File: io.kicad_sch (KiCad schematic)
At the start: 67 parts, among them J10 JP_REL1_COM_12V, J12 JP_REL2_COM_12V, J13 JP_REL3_COM_12V, J14 Conn_REL1, J15 Conn_REL2, J16 Conn_REL3, J5 JP_REL4_COM_12V, J8 JP_REL5_COM_12V, J9 JP_REL6_COM_12V, K2 TIANBO-HJR-4102-L, K3 TIANBO-HJR-4102-L, K4 TIANBO-HJR-4102-L, K5 TIANBO-HJR-4102-L, K6 TIANBO-HJR-4102-L, K7 TIANBO-HJR-4102-L, Q2 BSS138, Q3 BSS138, Q4 BSS138, Q5 BSS138, Q6 BSS138, Q7 BSS138, U10 74HC595, U20 HC 151, X5 Conn_Rel2, X6 Conn_Rel1

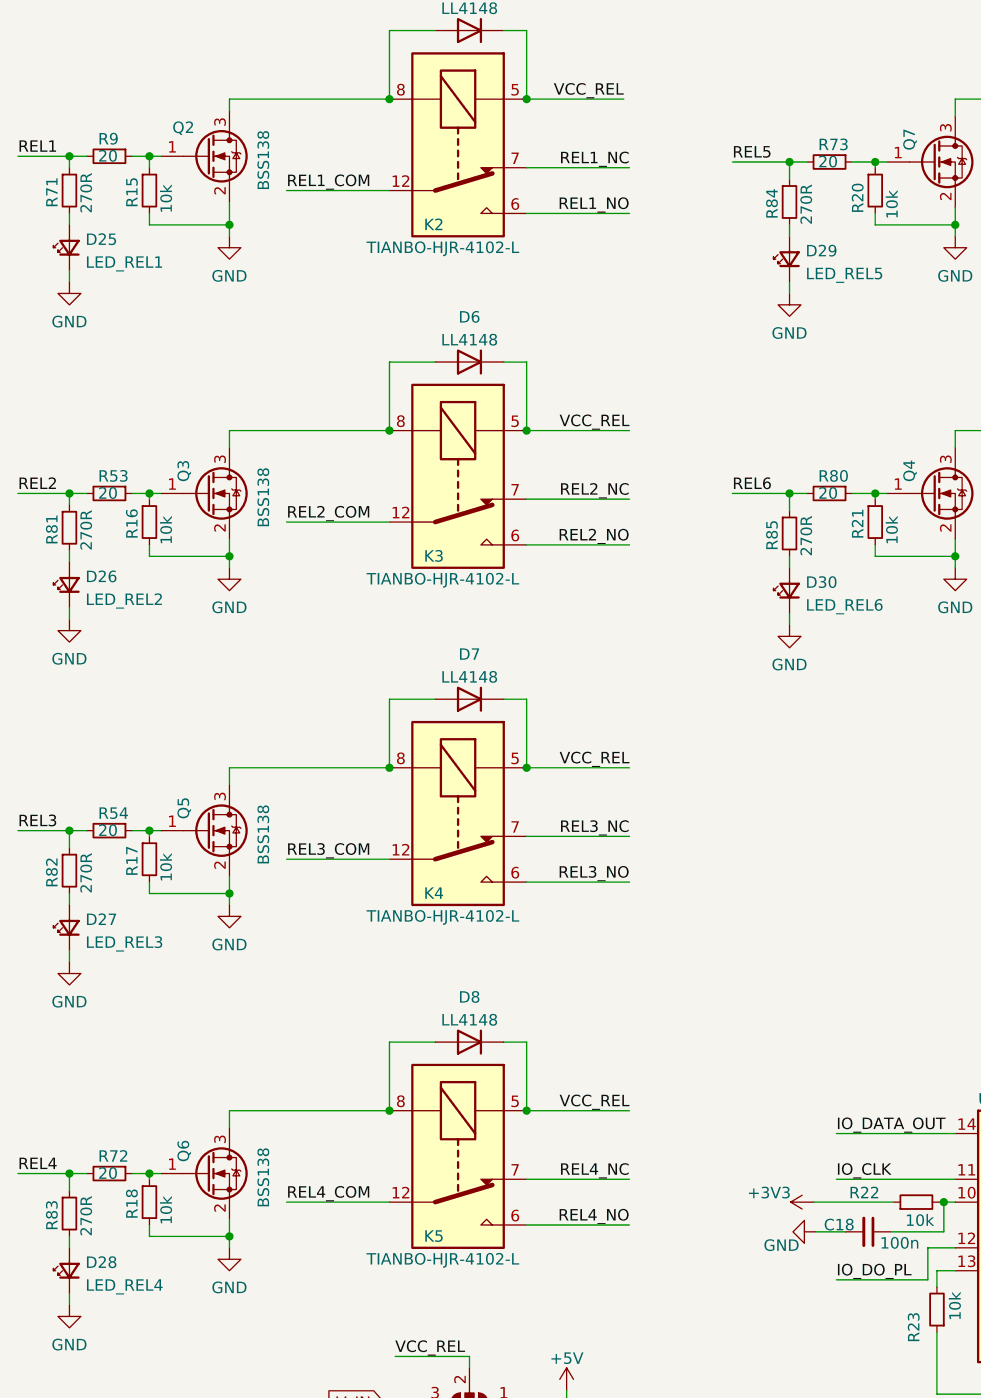
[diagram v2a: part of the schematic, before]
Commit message: Change extension bus
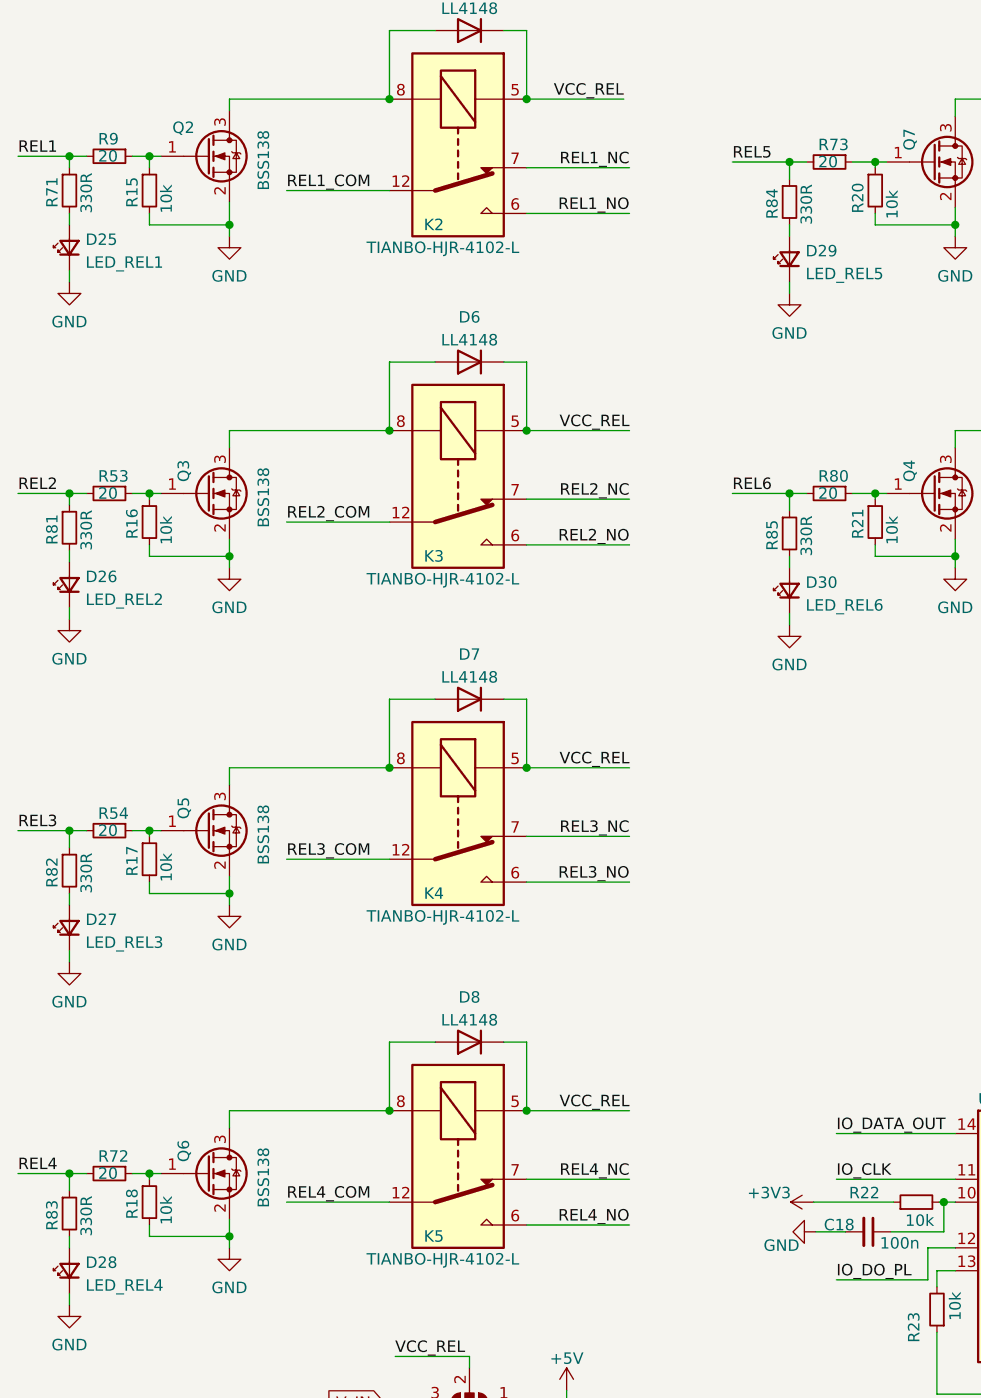
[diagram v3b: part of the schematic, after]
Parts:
- J10, J12, J13, J5, J8, J9: footprint Connector_PinHeader_2.54mm:PinHeader_1x02_P2.54mm_Vertical -> custom_th:PinHeader_1x02_P2.54mm_Vertical_jlc
- J14, J15, J16: footprint Connector_PinHeader_2.54mm:PinHeader_1x03_P2.54mm_Vertical -> custom_th:PinHeader_1x03_P2.54mm_Vertical_jlc
- R71, R81, R82, R83, R84, R85: value 270R -> 330R
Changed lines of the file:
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@@
   (title_block
     (title "BSC")
-    (date "2022-12-16")
-    (rev "2.1")
+    (date "2023-03-30")
+    (rev "2.3")
   )
   (junction (at 128.905 174.371) (diameter 0) (color 0 0 0 0)
@@
     (property "Reference" "J9" (id 0) (at 184.785 72.39 0))
     (property "Value" "JP_REL6_COM_12V" (id 1) (at 187.325 69.215 0))
-    (property "Footprint" "Connector_PinHeader_2.54mm:PinHeader_1x02_P2.54mm_Vertical" (id 2) (at 188.595 70.485 0)
+    (property "Footprint" "custom_th:PinHeader_1x02_P2.54mm_Vertical_jlc" (id 2) (at 188.595 70.485 0)
       (effects (font (size 1.27 1.27)) hide)
     )
@@
       (effects (font (size 1.27 1.27)) (justify left))
     )
-    (property "Value" "270R" (id 1) (at 22.225 118.745 90)
+    (property "Value" "330R" (id 1) (at 22.225 118.745 90)
       (effects (font (size 1.27 1.27)) (justify left))
     )
@@
     (property "Reference" "J12" (id 0) (at 184.785 38.735 0))
     (property "Value" "JP_REL2_COM_12V" (id 1) (at 187.96 36.195 0))
-    (property "Footprint" "Connector_PinHeader_2.54mm:PinHeader_1x02_P2.54mm_Vertical" (id 2) (at 189.23 37.465 0)
+    (property "Footprint" "custom_th:PinHeader_1x02_P2.54mm_Vertical_jlc" (id 2) (at 189.23 37.465 0)
       (effects (font (size 1.27 1.27)) hide)
     )
@@
       (effects (font (size 1.27 1.27)) (justify left))
     )
-    (property "Value" "270R" (id 1) (at 102.235 81.28 90)
+    (property "Value" "330R" (id 1) (at 102.235 81.28 90)
       (effects (font (size 1.27 1.27)) (justify left))
     )
@@
     (property "Reference" "J10" (id 0) (at 184.785 30.48 0))
     (property "Value" "JP_REL1_COM_12V" (id 1) (at 187.96 27.94 0))
-    (property "Footprint" "Connector_PinHeader_2.54mm:PinHeader_1x02_P2.54mm_Vertical" (id 2) (at 189.23 29.21 0)
+    (property "Footprint" "custom_th:PinHeader_1x02_P2.54mm_Vertical_jlc" (id 2) (at 189.23 29.21 0)
       (effects (font (size 1.27 1.27)) hide)
     )
@@
     (property "Reference" "J8" (id 0) (at 184.785 63.5 0))
     (property "Value" "JP_REL5_COM_12V" (id 1) (at 187.325 60.96 0))
-    (property "Footprint" "Connector_PinHeader_2.54mm:PinHeader_1x02_P2.54mm_Vertical" (id 2) (at 188.595 62.23 0)
+    (property "Footprint" "custom_th:PinHeader_1x02_P2.54mm_Vertical_jlc" (id 2) (at 188.595 62.23 0)
       (effects (font (size 1.27 1.27)) hide)
     )
@@
     (property "Reference" "J5" (id 0) (at 184.785 55.245 0))
     (property "Value" "JP_REL4_COM_12V" (id 1) (at 187.325 52.705 0))
-    (property "Footprint" "Connector_PinHeader_2.54mm:PinHeader_1x02_P2.54mm_Vertical" (id 2) (at 188.595 53.975 0)
+    (property "Footprint" "custom_th:PinHeader_1x02_P2.54mm_Vertical_jlc" (id 2) (at 188.595 53.975 0)
       (effects (font (size 1.27 1.27)) hide)
     )
@@
     (property "Reference" "J16" (id 0) (at 216.535 98.425 0))
     (property "Value" "Conn_REL3" (id 1) (at 212.725 102.87 0))
-    (property "Footprint" "Connector_PinHeader_2.54mm:PinHeader_1x03_P2.54mm_Vertical" (id 2) (at 213.36 98.425 0)
+    (property "Footprint" "custom_th:PinHeader_1x03_P2.54mm_Vertical_jlc" (id 2) (at 213.36 98.425 0)
       (effects (font (size 1.27 1.27)) hide)
     )
@@
     (property "Reference" "J14" (id 0) (at 216.535 121.285 0))
     (property "Value" "Conn_REL1" (id 1) (at 212.725 125.73 0))
-    (property "Footprint" "Connector_PinHeader_2.54mm:PinHeader_1x03_P2.54mm_Vertical" (id 2) (at 213.36 121.285 0)
+    (property "Footprint" "custom_th:PinHeader_1x03_P2.54mm_Vertical_jlc" (id 2) (at 213.36 121.285 0)
       (effects (font (size 1.27 1.27)) hide)
     )
@@
       (effects (font (size 1.27 1.27)) (justify left))
     )
-    (property "Value" "270R" (id 1) (at 22.225 156.845 90)
+    (property "Value" "330R" (id 1) (at 22.225 156.845 90)
       (effects (font (size 1.27 1.27)) (justify left))
     )
@@
       (effects (font (size 1.27 1.27)) (justify left))
     )
-    (property "Value" "270R" (id 1) (at 102.235 44.45 90)
+    (property "Value" "330R" (id 1) (at 102.235 44.45 90)
       (effects (font (size 1.27 1.27)) (justify left))
     )
@@
       (effects (font (size 1.27 1.27)) (justify left))
     )
-    (property "Value" "270R" (id 1) (at 22.225 80.645 90)
+    (property "Value" "330R" (id 1) (at 22.225 80.645 90)
       (effects (font (size 1.27 1.27)) (justify left))
     )
@@
     (property "Reference" "J13" (id 0) (at 184.785 47.625 0))
     (property "Value" "JP_REL3_COM_12V" (id 1) (at 187.325 44.45 0))
-    (property "Footprint" "Connector_PinHeader_2.54mm:PinHeader_1x02_P2.54mm_Vertical" (id 2) (at 189.23 45.72 0)
+    (property "Footprint" "custom_th:PinHeader_1x02_P2.54mm_Vertical_jlc" (id 2) (at 189.23 45.72 0)
       (effects (font (size 1.27 1.27)) hide)
     )
@@
     (property "Reference" "J15" (id 0) (at 216.535 109.855 0))
     (property "Value" "Conn_REL2" (id 1) (at 212.725 114.3 0))
-    (property "Footprint" "Connector_PinHeader_2.54mm:PinHeader_1x03_P2.54mm_Vertical" (id 2) (at 213.36 109.855 0)
+    (property "Footprint" "custom_th:PinHeader_1x03_P2.54mm_Vertical_jlc" (id 2) (at 213.36 109.855 0)
       (effects (font (size 1.27 1.27)) hide)
     )
@@
       (effects (font (size 1.27 1.27)) (justify left))
     )
-    (property "Value" "270R" (id 1) (at 22.225 43.18 90)
-      (effects (font (size 1.27 1.27)) (justify left))
-    )
+    (property "Value" "330R" (id 1) (at 22.225 43.18 90)
+      (effects (font (size 1.27 1.27)) (justify left))
+    )

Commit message: Ref 2.4
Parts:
- removed JP29: JP_REL_VCC, Jumper:SolderJumper-3_P1.3mm_Open_RoundedPad1.0x1.5mm, symbol Jumper:SolderJumper_3_Open
- added JP29: JP_REL_VCC, Jumper:SolderJumper-3_P1.3mm_Bridged12_RoundedPad1.0x1.5mm_NumberLabels, symbol Jumper:SolderJumper_3_Bridged12
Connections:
- net +5V: now also JP29.1 (A)
- net VCC_REL: now also JP29.2 (C)
- net V_IN: now also JP29.3 (B)
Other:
- note added: "Je nach Relaistyp kann eine Spulenspannung von 5V oder 12V gewählt werden. Wichtig hierfür ist, dass die Bestückung der DC/DC auf Seite beachtet wird."
- note removed: "Je nach Relaistyp kann eine Spulenspannung von 5V oder 12V gewählt werden. Wichtig hierfür ist, dass die Bestückung der DC/DC auf Seite beachtet wrid."
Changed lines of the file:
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@@
   (title_block
     (title "BSC")
-    (date "2023-03-30")
-    (rev "2.3")
+    (date "2023-06-25")
+    (rev "2.4")
   )
   (junction (at 128.905 174.371) (diameter 0) (color 0 0 0 0)
@@
     (stroke (width 0) (type default) (color 0 0 0 0))
   )
+  (wire (pts (xy 64.77 180.975) (xy 64.77 179.07))
+    (stroke (width 0) (type default) (color 0 0 0 0))
+  )
   (wire (pts (xy 152.4 59.69) (xy 152.4 67.31))
     (stroke (width 0) (type default) (color 0 0 0 0))
@@
     (stroke (width 0) (type default) (color 0 0 0 0))
   )
+  (wire (pts (xy 55.245 180.975) (xy 64.77 180.975))
+    (stroke (width 0) (type default) (color 0 0 0 0))
+  )
   (wire (pts (xy 125.73 77.47) (xy 137.16 77.47))
     (stroke (width 0) (type default) (color 0 0 0 0))
@@
     (stroke (width 0) (type default) (color 0 0 0 0))
   )
-  (wire (pts (xy 64.77 170.18) (xy 64.77 171.45))
-    (stroke (width 0) (type default) (color 0 0 0 0))
-  )
   (wire (pts (xy 118.745 158.115) (xy 115.697 158.115))
     (stroke (width 0) (type default) (color 0 0 0 0))
   )
+  (wire (pts (xy 55.245 173.355) (xy 55.245 175.26))
+    (stroke (width 0) (type default) (color 0 0 0 0))
+  )
   (wire (pts (xy 193.675 53.975) (xy 208.28 53.975))
     (stroke (width 0) (type default) (color 0 0 0 0))
@@
     (stroke (width 0) (type default) (color 0 0 0 0))
   )
-  (wire (pts (xy 56.515 170.18) (xy 64.77 170.18))
-    (stroke (width 0) (type default) (color 0 0 0 0))
-  )
   (wire (pts (xy 208.28 107.315) (xy 192.405 107.315))
     (stroke (width 0) (type default) (color 0 0 0 0))
   )
-  (wire (pts (xy 75.565 175.26) (xy 75.565 173.99))
-    (stroke (width 0) (type default) (color 0 0 0 0))
-  )
   (wire (pts (xy 139.065 155.575) (xy 149.225 155.575))
     (stroke (width 0) (type default) (color 0 0 0 0))
@@
     (stroke (width 0) (type default) (color 0 0 0 0))
   )
-  (text "Je nach Relaistyp kann eine Spulenspannung\nvon 5V oder 12V gewählt werden. \nWichtig hierfür ist, dass die Bestückung der \nDC/DC auf Seite beachtet wrid.\n"
+  (text "Je nach Relaistyp kann eine Spulenspannung\nvon 5V oder 12V gewählt werden. \nWichtig hierfür ist, dass die Bestückung der \nDC/DC auf Seite beachtet wird.\n"
     (at 45.72 191.135 0)
     (effects (font (size 1.27 1.27)) (justify left bottom))
@@
     (effects (font (size 1.27 1.27)) (justify left bottom))
   )
-  (label "VCC_REL" (at 56.515 170.18 0)
+  (label "VCC_REL" (at 55.245 180.975 0)
     (effects (font (size 1.27 1.27)) (justify left bottom))
   )
@@
     )
   )
-  (global_label "V_IN" (shape input) (at 55.245 175.26 180) (fields_autoplaced)
-    (effects (font (size 1.27 1.27)) (justify right))
-    (property "Intersheet References" "${INTERSHEET_REFS}" (id 0) (at 48.8405 175.3394 0)
-      (effects (font (size 1.27 1.27)) (justify right) hide)
+  (global_label "V_IN" (shape input) (at 75.565 175.26 0) (fields_autoplaced)
+    (effects (font (size 1.27 1.27)) (justify left))
+    (property "Intersheet References" "${INTERSHEET_REFS}" (id 0) (at 81.9695 175.1806 0)
+      (effects (font (size 1.27 1.27)) (justify left) hide)
     )
   )
@@
     (pin "1")
     (pin "2")
+  )
+  (symbol (lib_id "Jumper:SolderJumper_3_Bridged12") (at 64.77 175.26 0) (unit 1)
+    (in_bom yes) (on_board yes) (fields_autoplaced)
+    (property "Reference" "JP29" (id 0) (at 64.77 170.6712 0))
+    (property "Value" "JP_REL_VCC" (id 1) (at 64.77 173.2081 0))
+    (property "Footprint" "Jumper:SolderJumper-3_P1.3mm_Bridged12_RoundedPad1.0x1.5mm_NumberLabels" (id 2) (at 64.77 175.26 0)
+      (effects (font (size 1.27 1.27)) hide)
+    )
+    (property "Datasheet" "~" (id 3) (at 64.77 175.26 0)
+      (effects (font (size 1.27 1.27)) hide)
+    )
+    (pin "1")
+    (pin "2")
+    (pin "3")
   )
   (symbol (lib_id "Transistor_FET:BSS138") (at 116.205 74.295 0) (unit 1)
@@
     (pin "1")
   )
-  (symbol (lib_id "power:+5V") (at 75.565 173.99 0) (unit 1)
-    (in_bom yes) (on_board yes)
-    (property "Reference" "#PWR016" (id 0) (at 75.565 177.8 0)
-      (effects (font (size 1.27 1.27)) hide)
-    )
-    (property "Value" "+5V" (id 1) (at 75.565 170.4142 0))
-    (property "Footprint" "" (id 2) (at 75.565 173.99 0)
-      (effects (font (size 1.27 1.27)) hide)
-    )
-    (property "Datasheet" "" (id 3) (at 75.565 173.99 0)
+  (symbol (lib_id "power:+5V") (at 55.245 173.355 0) (unit 1)
+    (in_bom yes) (on_board yes)
+    (property "Reference" "#PWR016" (id 0) (at 55.245 177.165 0)
+      (effects (font (size 1.27 1.27)) hide)
+    )
+    (property "Value" "+5V" (id 1) (at 55.245 169.7792 0))
+    (property "Footprint" "" (id 2) (at 55.245 173.355 0)
+      (effects (font (size 1.27 1.27)) hide)
+    )
+    (property "Datasheet" "" (id 3) (at 55.245 173.355 0)
       (effects (font (size 1.27 1.27)) hide)
     )
@@
     (pin "1")
   )
-  (symbol (lib_id "Jumper:SolderJumper_3_Open") (at 64.77 175.26 180) (unit 1)
-    (in_bom yes) (on_board yes) (fields_autoplaced)
-    (property "Reference" "JP29" (id 0) (at 64.77 178.1794 0))
-    (property "Value" "JP_REL_VCC" (id 1) (at 64.77 180.7163 0))
-    (property "Footprint" "Jumper:SolderJumper-3_P1.3mm_Open_RoundedPad1.0x1.5mm" (id 2) (at 64.77 175.26 0)
-      (effects (font (size 1.27 1.27)) hide)
-    )
-    (property "Datasheet" "~" (id 3) (at 64.77 175.26 0)
-      (effects (font (size 1.27 1.27)) hide)
-    )
-    (pin "1")
-    (pin "2")
-    (pin "3")
-  )
   (symbol (lib_id "Device:R_Small") (at 231.14 152.4 180) (unit 1)
